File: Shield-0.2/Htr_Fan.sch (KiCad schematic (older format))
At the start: 23 parts, among them J27 TP

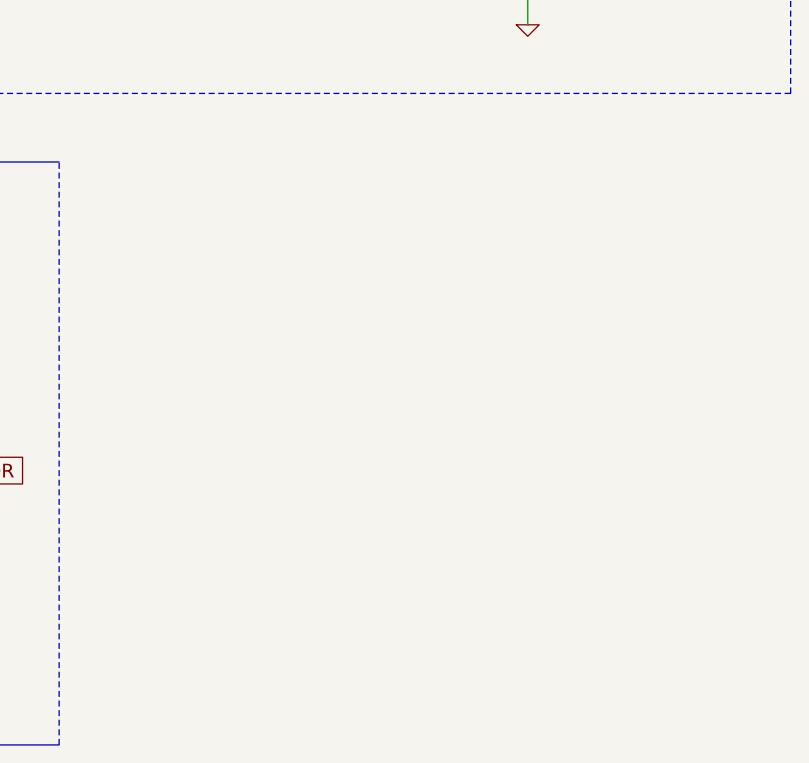
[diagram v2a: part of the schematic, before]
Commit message: Tell-tale LEDs added to shield.
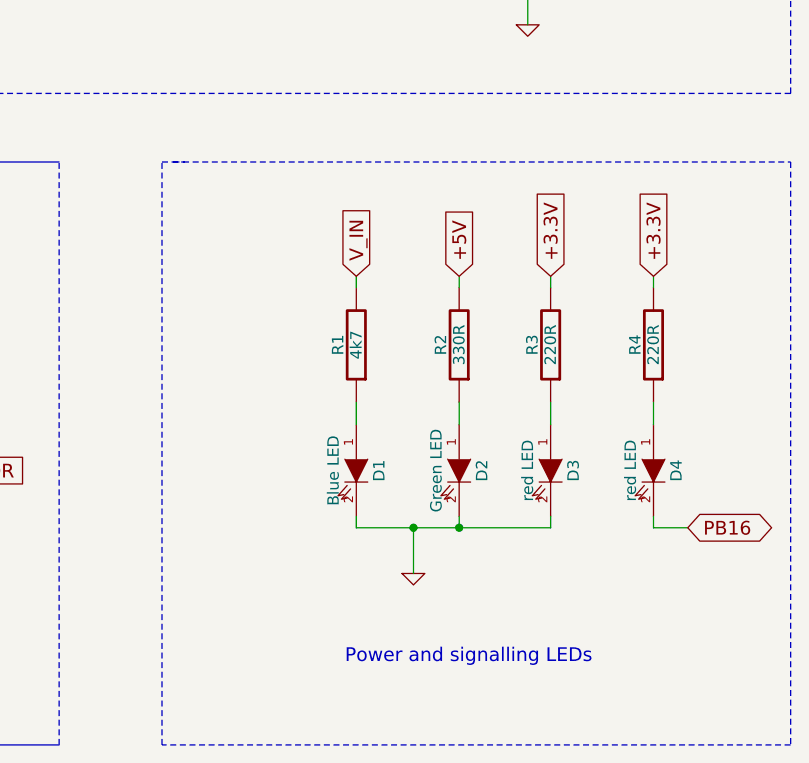
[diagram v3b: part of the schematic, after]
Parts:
- added D1: Blue LED, symbol LED
- added D2: Green LED, symbol LED
- added D3, D4: red LED, symbol LED
- added R1: 4k7, symbol R
- added R2: 330R, symbol R
- added R3, R4: 220R, symbol R
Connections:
- net +3.3V: now also R3.2, R4.2
- net +5V: now also R2.2
- net GND: now also D1.2 (K), D2.2 (K), D3.2 (K)
- net V_IN: now also R1.2
- new net: D1.1 (A), R1.1
- new net: D2.1 (A), R2.1
- new net: D3.1 (A), R3.1
- new net: D4.1 (A), R4.1
- new net PB16: D4.2 (K)
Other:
- note added: "Power and signalling LEDs"
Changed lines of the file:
@@
 $EndComp
 $Comp
-L GND #PWR25
+L GND #PWR024
 U 1 1 50905416
 P 7400 4450
-F 0 "#PWR25" H 7400 4450 30  0001 C CNN
+F 0 "#PWR024" H 7400 4450 30  0001 C CNN
 F 1 "GND" H 7400 4380 30  0001 C CNN
 F 2 "" H 7400 4450 60  0001 C CNN
@@
 E1-
 $Comp
-L GND #PWR24
+L GND #PWR025
 U 1 1 5064BB75
 P 3300 4450
-F 0 "#PWR24" H 3300 4450 30  0001 C CNN
+F 0 "#PWR025" H 3300 4450 30  0001 C CNN
 F 1 "GND" H 3300 4380 30  0001 C CNN
 F 2 "" H 3300 4450 60  0001 C CNN
@@
 Text GLabel 2250 1800 1    60   Input ~ 0
 +5V
+Wire Wire Line
+	6650 6650 6650 6600
+Wire Wire Line
+	6650 5550 6650 5600
+Wire Wire Line
+	6650 6100 6650 6200
+$Comp
+L LED D1
+U 1 1 54916E1F
+P 6650 6400
+F 0 "D1" H 6650 6500 50  0000 C CNN
+F 1 "Blue LED" H 6650 6300 50  0000 C CNN
+F 2 "" H 6650 6400 60  0001 C CNN
+F 3 "" H 6650 6400 60  0001 C CNN
+	1    6650 6400
+	0    1    1    0
+$EndComp
+$Comp
+L R R1
+U 1 1 54916E25
+P 6650 5850
+F 0 "R1" V 6730 5850 50  0000 C CNN
+F 1 "4k7" V 6650 5850 50  0000 C CNN
+F 2 "" H 6650 5850 60  0001 C CNN
+F 3 "" H 6650 5850 60  0001 C CNN
+	1    6650 5850
+	-1   0    0    1
+$EndComp
+Wire Wire Line
+	7100 6650 7100 6600
+Wire Wire Line
+	7100 5550 7100 5600
+Wire Wire Line
+	7100 6100 7100 6200
+$Comp
+L LED D2
+U 1 1 54916E46
+P 7100 6400
+F 0 "D2" H 7100 6500 50  0000 C CNN
+F 1 "Green LED" H 7100 6300 50  0000 C CNN
+F 2 "" H 7100 6400 60  0001 C CNN
+F 3 "" H 7100 6400 60  0001 C CNN
+	1    7100 6400
+	0    1    1    0
+$EndComp
+$Comp
+L R R2
+U 1 1 54916E4C
+P 7100 5850
+F 0 "R2" V 7180 5850 50  0000 C CNN
+F 1 "330R" V 7100 5850 50  0000 C CNN
+F 2 "" H 7100 5850 60  0001 C CNN
+F 3 "" H 7100 5850 60  0001 C CNN
+	1    7100 5850
+	-1   0    0    1
+$EndComp
+Wire Wire Line
+	7500 6650 7500 6600
+Wire Wire Line
+	7500 5550 7500 5600
+Wire Wire Line
+	7500 6100 7500 6200
+$Comp
+L LED D3
+U 1 1 54916E55
+P 7500 6400
+F 0 "D3" H 7500 6500 50  0000 C CNN
+F 1 "red LED" H 7500 6300 50  0000 C CNN
+F 2 "" H 7500 6400 60  0001 C CNN
+F 3 "" H 7500 6400 60  0001 C CNN
+	1    7500 6400
+	0    1    1    0
+$EndComp
+$Comp
+L R R3
+U 1 1 54916E5B
+P 7500 5850
+F 0 "R3" V 7580 5850 50  0000 C CNN
+F 1 "220R" V 7500 5850 50  0000 C CNN
+F 2 "" H 7500 5850 60  0001 C CNN
+F 3 "" H 7500 5850 60  0001 C CNN
+	1    7500 5850
+	-1   0    0    1
+$EndComp
+Text GLabel 6650 5550 1    60   Input ~ 0
+V_IN
+Text GLabel 7100 5550 1    60   Input ~ 0
++5V
+Text GLabel 7500 5550 1    60   Input ~ 0
++3.3V
+Wire Wire Line
+	6650 6650 7500 6650
+Connection ~ 7100 6650
+Wire Wire Line
+	6900 6650 6900 6850
+Connection ~ 6900 6650
+$Comp
+L GND #PWR026
+U 1 1 54916FD4
+P 6900 6850
+F 0 "#PWR026" H 6900 6850 30  0001 C CNN
+F 1 "GND" H 6900 6780 30  0001 C CNN
+F 2 "" H 6900 6850 60  0001 C CNN
+F 3 "" H 6900 6850 60  0001 C CNN
+	1    6900 6850
+	1    0    0    -1
+$EndComp
+Wire Wire Line
+	7950 6650 7950 6600
+Wire Wire Line
+	7950 5550 7950 5600
+Wire Wire Line
+	7950 6100 7950 6200
+$Comp
+L LED D4
+U 1 1 54916FDD
+P 7950 6400
+F 0 "D4" H 7950 6500 50  0000 C CNN
+F 1 "red LED" H 7950 6300 50  0000 C CNN
+F 2 "" H 7950 6400 60  0001 C CNN
+F 3 "" H 7950 6400 60  0001 C CNN
+	1    7950 6400
+	0    1    1    0
+$EndComp
+$Comp
+L R R4
+U 1 1 54916FE3
+P 7950 5850
+F 0 "R4" V 8030 5850 50  0000 C CNN
+F 1 "220R" V 7950 5850 50  0000 C CNN
+F 2 "" H 7950 5850 60  0001 C CNN
+F 3 "" H 7950 5850 60  0001 C CNN
+	1    7950 5850
+	-1   0    0    1
+$EndComp
+Text GLabel 7950 5550 1    60   Input ~ 0
++3.3V
+Wire Notes Line
+	5850 5050 8550 5050
+Wire Notes Line
+	8550 5050 8550 7600
+Wire Notes Line
+	8550 7600 5800 7600
+Wire Notes Line
+	5800 7600 5800 5050
+Wire Notes Line
+	5800 5050 5900 5050
+Text Notes 6600 7250 0    60   ~ 0
+Power and signalling LEDs
+Text GLabel 8100 6650 2    60   BiDi ~ 0
+PB16
+Wire Wire Line
+	8100 6650 7950 6650
 $EndSCHEMATC

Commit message: Updating Duet 0.7a...
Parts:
- R2: value 330R -> 680R
- R3, R4: value 220R -> 470R
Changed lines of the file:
@@
 LIBS:FE
 LIBS:Shield-cache
-EELAYER 24 0
+EELAYER 27 0
 EELAYER END
 $Descr A3 16535 11693
@@
 Sheet 4 4
 Title "Duet"
-Date "16 dec 2014"
+Date "17 dec 2014"
 Rev "0.7"
 Comp "Think3DPrint3D, RepRapPro"
@@
 P 7100 5850
 F 0 "R2" V 7180 5850 50  0000 C CNN
-F 1 "330R" V 7100 5850 50  0000 C CNN
+F 1 "680R" V 7100 5850 50  0000 C CNN
 F 2 "" H 7100 5850 60  0001 C CNN
 F 3 "" H 7100 5850 60  0001 C CNN
@@
 P 7500 5850
 F 0 "R3" V 7580 5850 50  0000 C CNN
-F 1 "220R" V 7500 5850 50  0000 C CNN
+F 1 "470R" V 7500 5850 50  0000 C CNN
 F 2 "" H 7500 5850 60  0001 C CNN
 F 3 "" H 7500 5850 60  0001 C CNN
@@
 P 7950 5850
 F 0 "R4" V 8030 5850 50  0000 C CNN
-F 1 "220R" V 7950 5850 50  0000 C CNN
+F 1 "470R" V 7950 5850 50  0000 C CNN
 F 2 "" H 7950 5850 60  0001 C CNN
 F 3 "" H 7950 5850 60  0001 C CNN
